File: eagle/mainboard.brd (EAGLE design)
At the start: 100.2 x 100 mm, 100 parts, among them IC1 74HC02D, IC2 74HC151D, IC3 74HC151D, IC4 74HC590D

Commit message: usb change
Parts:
- removed CONTROLLER-IN, POWER-IN, USB-CONTROLLER1, USB-CONTROLLER2, USB-CONTROLLER3, USB-CONTROLLER4: 632723100011_USBC_3.1, Eagle_WR-USB (rev22c):632723100011_USBC_3.1
- removed R55, R70: 5k1Ω, rcl:R0805
- removed R57, R58, R59, R60: 56kΩ, rcl:R0805
- added USBC1-2, USB_C3-4: 61400826021, Wurth_Connectors_WR-USB:61400826021
- added USBCIN, USBPOWER: 61410416121R, Wurth_Connectors_WR-USB:61410416121R
- moved C_DATA_1 57.7 mm to (17.2, 7.00), turned to 270 degrees
- moved R3 44.6 mm to (3.50, 11.2), flipped to the bottom
- moved C4 44.6 mm to (3.50, 9.00), flipped to the bottom
- moved R21 43.6 mm to (25.8, 22.8), flipped to the bottom, turned to 180 degrees
- moved C_DATA_2 36.3 mm to (17.2, 15.0), turned to 90 degrees
- moved C2 32.7 mm to (3.50, 6.50), flipped to the bottom
- moved R2 28.2 mm to (3.50, 13.5), flipped to the bottom
- moved R22 28.1 mm to (25.8, 26.2), turned to 180 degrees
- moved R4 22.3 mm to (3.50, 31.2), flipped to the bottom
- moved R25 20.7 mm to (25.8, 32.8), turned to 180 degrees
- moved C3 18.3 mm to (3.50, 24.5), flipped to the bottom
- moved C_DATA_4 18.0 mm to (17.2, 32.8), turned to 90 degrees
- moved R24 16.8 mm to (25.8, 29.2), turned to 180 degrees
- moved C_DATA_3 16.1 mm to (17.2, 24.8), turned to 270 degrees
- moved C1 10.1 mm to (3.50, 26.8), flipped to the bottom
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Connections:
- removed net N$1: POWER-IN.A4, POWER-IN.A9, R5.1
- removed net N$13: R58.2, USB-CONTROLLER4.A5
- removed net N$14: R59.2, USB-CONTROLLER3.A5
- removed net N$31: R60.2, USB-CONTROLLER2.A5
- removed net N$32: CONTROLLER-IN.A4, CONTROLLER-IN.A9, R71.1
- removed net N$33: CONTROLLER-IN.A5, R70.2
- removed net N$6: R57.2, USB-CONTROLLER1.A5
- new net N$7: R1.1, USB_C3-4.1
- net +5V: no longer R57.1, R58.1, R59.1, R60.1
- net C1_DATA: now also USBC1-2.2; no longer USB-CONTROLLER1.A6
- net C2_DATA: now also USBC1-2.6; no longer USB-CONTROLLER2.A6
- net C3_DATA: now also USB_C3-4.2; no longer USB-CONTROLLER3.A6
- net C4_DATA: now also USB_C3-4.6; no longer USB-CONTROLLER4.A6
- net CONTROLLER_CLOCK: now also USBCIN.3; no longer CONTROLLER-IN.A7
- net CONTROLLER_OUT: now also USBCIN.2; no longer CONTROLLER-IN.A6
- net C_CLOCK: now also USBC1-2.3, USBC1-2.7, USB_C3-4.3, USB_C3-4.7; no longer USB-CONTROLLER1.A7, USB-CONTROLLER2.A7, USB-CONTROLLER3.A7, USB-CONTROLLER4.A7
- net GND: now also USBC1-2.4, USBC1-2.8, USBC1-2.S1, USBC1-2.S2, USBC1-2.S3, USBC1-2.S4, USBPOWER.4, USBPOWER.S1, USBPOWER.S2, USB_C3-4.4, USB_C3-4.8, USB_C3-4.S1, USB_C3-4.S2, USB_C3-4.S3, USB_C3-4.S4; no longer POWER-IN.A1, POWER-IN.A10, POWER-IN.A11, POWER-IN.A12, POWER-IN.A2, POWER-IN.A3, POWER-IN.A6, POWER-IN.A7, POWER-IN.A8, R55.1, USB-CONTROLLER1.A1, USB-CONTROLLER1.A10, USB-CONTROLLER1.A11, USB-CONTROLLER1.A12, USB-CONTROLLER1.A2, USB-CONTROLLER1.A3, USB-CONTROLLER1.A8, USB-CONTROLLER2.A1, USB-CONTROLLER2.A10, USB-CONTROLLER2.A11, USB-CONTROLLER2.A12, USB-CONTROLLER2.A2, USB-CONTROLLER2.A3, USB-CONTROLLER2.A8, USB-CONTROLLER3.A1, USB-CONTROLLER3.A10, USB-CONTROLLER3.A11, USB-CONTROLLER3.A12, USB-CONTROLLER3.A2, USB-CONTROLLER3.A3, USB-CONTROLLER3.A8, USB-CONTROLLER4.A1, USB-CONTROLLER4.A10, USB-CONTROLLER4.A11, USB-CONTROLLER4.A12, USB-CONTROLLER4.A2, USB-CONTROLLER4.A3, USB-CONTROLLER4.A8
- net GNDA: now also USBCIN.4, USBCIN.S1, USBCIN.S2; no longer CONTROLLER-IN.A1, CONTROLLER-IN.A10, CONTROLLER-IN.A11, CONTROLLER-IN.A12, CONTROLLER-IN.A2, CONTROLLER-IN.A3, CONTROLLER-IN.A8, R70.1
- net N$2: now also USBC1-2.5; no longer USB-CONTROLLER2.A4, USB-CONTROLLER2.A9
- net N$3: now also R4.1, USB_C3-4.5; no longer R1.1, USB-CONTROLLER3.A4, USB-CONTROLLER3.A9
- net N$4: now also R3.1, USBC1-2.1; no longer R4.1, USB-CONTROLLER4.A4, USB-CONTROLLER4.A9
- net N$5: now also R71.1, USBCIN.1; no longer R3.1, USB-CONTROLLER1.A4, USB-CONTROLLER1.A9
- net N$8: now also R5.1, USBPOWER.1; no longer POWER-IN.A5, R55.2
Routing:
- net PA10_CPU: track 87.1 -> 30.8 mm
- net C_CLOCK: track 125.5 -> 79.7 mm, vias 11 -> 0
- net +5V: track 61.2 -> 17.0 mm, vias 2 -> 0
- net PA9_CPU: track 75.4 -> 34.8 mm, vias 3 -> 0
- net PA10_CPU1: track 45.1 -> 23.1 mm
- net PA9_CPU1: track 42.4 -> 27.1 mm
- net N$1: track 12.7 -> 0.00 mm
- net N$32: track 12.4 -> 0.00 mm, vias 2 -> 0
- net GND: track 22.8 -> 33.8 mm
- net C1: track 8.61 -> 19.3 mm, vias 1 -> 0
- net N$5: track 9.33 -> 0.00 mm, vias 2 -> 0
- net N$7: track 0.00 -> 9.09 mm
- net C2: track 6.00 -> 14.4 mm
- net C3_DATA: track 10.8 -> 5.24 mm
- net C1_DATA: track 10.7 -> 5.24 mm
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
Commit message: board changes
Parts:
- moved USBCIN 16.6 mm to (126.0, -7.25), flipped to the bottom
- moved R23 1.03 mm to (56.9, 38.5)
- moved 5V 0.75 mm to (94.2, 5.75)
- moved C5 0.75 mm to (80.0, 3.75)
- moved GND 0.75 mm to (94.2, 9.00)
- moved R5 0.75 mm to (80.0, 8.00)
- moved USBPOWER 0.75 mm to (91.5, 7.75)
- moved VGA 0.25 mm to (91.2, 34.8)
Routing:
- net GPU_READY: track 63.3 -> 69.8 mm
- net CONTROLLER_OUT: track 24.4 -> 19.9 mm
- net C_CLOCK: track 79.7 -> 78.8 mm
- net PA8_CPU: track 2.84 -> 3.50 mm
- net DOUBLE1: track 100.7 -> 100.1 mm

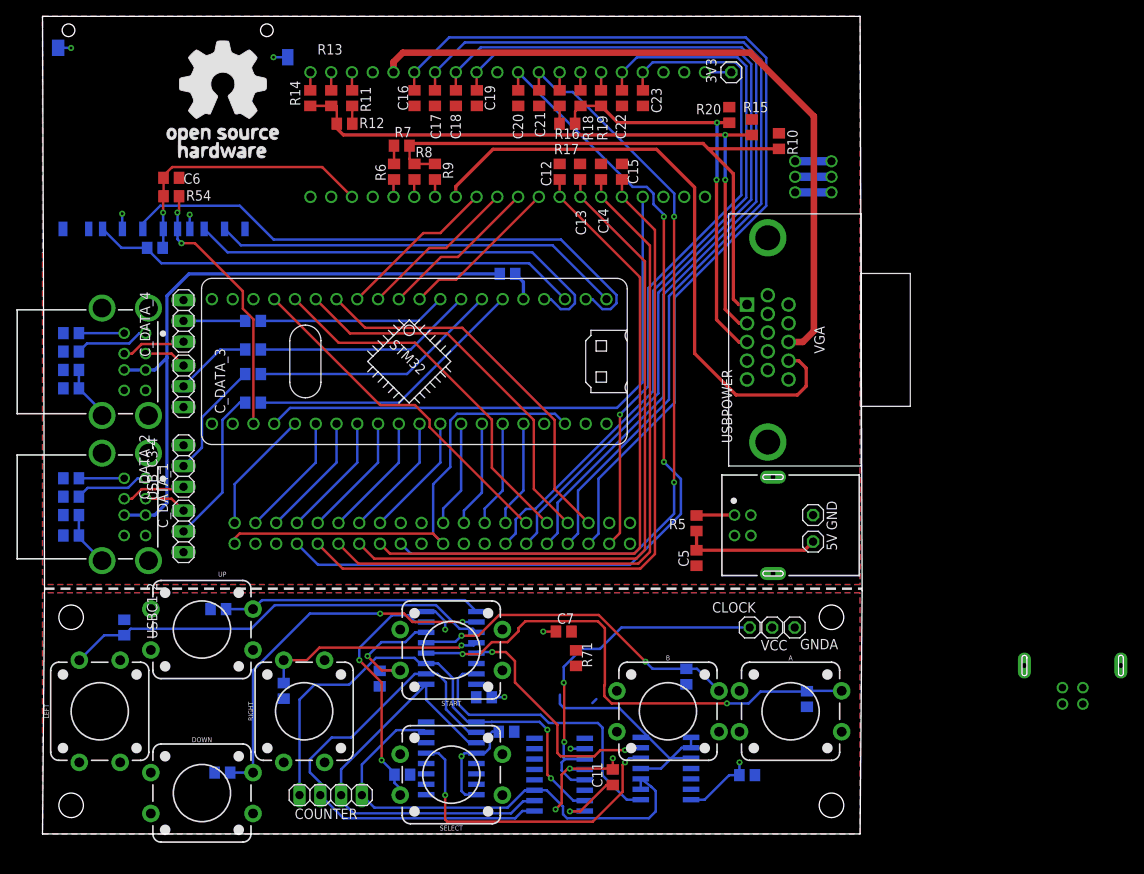
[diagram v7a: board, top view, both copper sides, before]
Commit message: positioned controller reciver, massive cleanup, simplified routes, moved labels
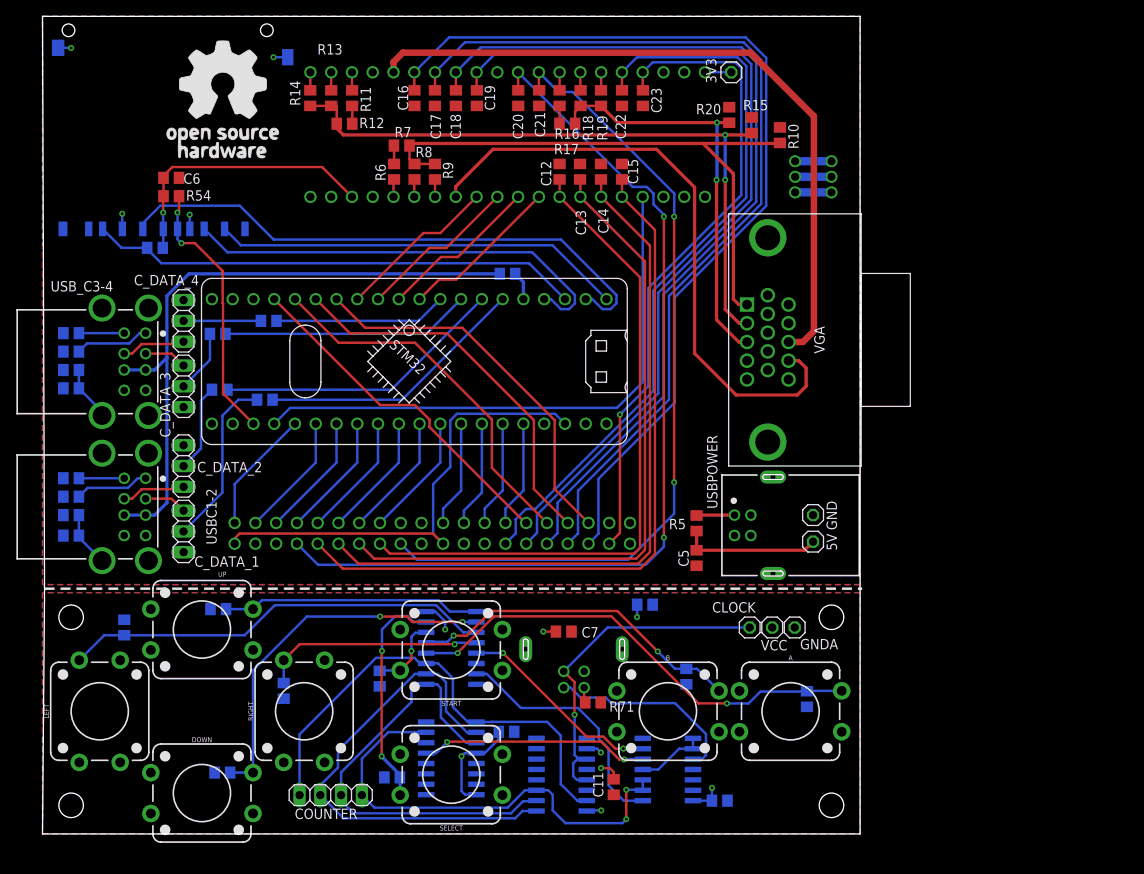
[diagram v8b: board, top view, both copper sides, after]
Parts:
- moved USBCIN 61.0 mm to (65.0, -5.25)
- moved C10 22.7 mm to (73.7, -1.96), turned to 180 degrees
- moved R71 5.80 mm to (67.3, -13.9), turned to 0 degrees
- moved R24 4.73 mm to (21.4, 31.2)
- moved C8 4.59 mm to (82.8, -25.9)
- moved R22 4.51 mm to (21.7, 24.3)
- moved R25 1.92 mm to (27.7, 32.8)
- moved R21 1.48 mm to (27.2, 23.1)
- moved R61 1.29 mm to (42.8, -23.1), turned to 0 degrees
- moved C11 1.21 mm to (69.9, -24.3)
- moved R10 0.73 mm to (90.2, 55.5)
- moved IC1 0.27 mm to (76.5, -22.1)
- moved IC4 0.24 mm to (63.5, -22.8)
- moved R15 0.24 mm to (86.8, 56.7)
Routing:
- net GNDA: track 16.7 -> 4.19 mm, vias 4 -> 2
- net VCC: track 37.3 -> 25.6 mm
- net N$11: track 39.2 -> 28.0 mm
- net START: track 15.6 -> 9.24 mm
- net N$29: track 36.3 -> 30.1 mm
- net PA10_CPU: track 30.8 -> 35.7 mm
- net A: track 62.5 -> 57.8 mm
- net CONTROLLER_OUT: track 19.9 -> 24.1 mm
- net N$15: track 29.4 -> 25.2 mm
- net C2: track 14.4 -> 10.8 mm
- net PA9_CPU1: track 27.1 -> 30.6 mm
- net SELECT: track 30.2 -> 27.6 mm
- net N$25: track 62.3 -> 60.2 mm
- net N$26: track 53.7 -> 55.7 mm
- net N$24: track 61.2 -> 59.2 mm, vias 2 -> 0
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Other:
- board size 100.2 x 100 mm -> 100 x 100 mm
